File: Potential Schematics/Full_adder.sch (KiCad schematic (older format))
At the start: 5 parts

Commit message: Made Full ALU
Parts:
- gave numbers to parts that had none: 2
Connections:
- net Cin: now also U2.13, U4.10 (IN2); no longer U2.2, U4.2 (IN2)
- net Cout: now also U4.11 (OUT); no longer U4.3 (OUT)
- net S: now also U4.8 (OUT); no longer U4.3 (OUT)
- net a: now also U2.9, U4.4 (IN1); no longer U2.1, U4.1 (IN1)
- net b: now also U2.10, U4.5 (IN2); no longer U2.2, U4.2 (IN2)
- new net: U2.8, U4.13 (IN2)
- new net: U2.12, U4.6 (OUT), U4.9 (IN1)
- new net: U2.11, U4.12 (IN1)
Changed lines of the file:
@@
 $Descr A4 11693 8268
 encoding utf-8
-Sheet 4 6
+Sheet 8 22
 Title "Full-Adder"
 Date ""
@@
 $Comp
 L 74LS08 U?
-U 1 1 5B98F241
+U 3 1 5B98F241
 P 3800 4700
 AR Path="/5B987476/5B988F04/5B98F241" Ref="U?"  Part="1"
-AR Path="/5B990C59/5B990C5E/5B988F04/5B98F241" Ref="U?"  Part="1"
-F 0 "U?" H 3800 4750 50  0000 C CNN
+AR Path="/5B990C59/5B990C5E/5B988F04/5B98F241" Ref="U2"  Part="2"
+AR Path="/5B990C59/5B99BC00/5B988F04/5B98F241" Ref="U5"  Part="3"
+AR Path="/5B990C59/5B99C896/5B988F04/5B98F241" Ref="U13"  Part="4"
+AR Path="/5B990C59/5B99C8B8/5B988F04/5B98F241" Ref="U28"  Part="1"
+F 0 "U5" H 3800 4750 50  0000 C CNN
 F 1 "74LS08" H 3800 4650 50  0000 C CNN
 F 2 "" H 3800 4700 50  0001 C CNN
 F 3 "" H 3800 4700 50  0001 C CNN
-	1    3800 4700
+	3    3800 4700
 	1    0    0    -1
 $EndComp
 $Comp
 L 74LS86 U?
-U 1 1 5B98F2D0
+U 2 1 5B98F2D0
 P 3800 2950
 AR Path="/5B987476/5B988F04/5B98F2D0" Ref="U?"  Part="1"
-AR Path="/5B990C59/5B990C5E/5B988F04/5B98F2D0" Ref="U?"  Part="1"
-F 0 "U?" H 3850 3000 50  0000 C CNN
+AR Path="/5B990C59/5B990C5E/5B988F04/5B98F2D0" Ref="U4"  Part="2"
+AR Path="/5B990C59/5B99BC00/5B988F04/5B98F2D0" Ref="U12"  Part="2"
+AR Path="/5B990C59/5B99C896/5B988F04/5B98F2D0" Ref="U20"  Part="2"
+AR Path="/5B990C59/5B99C8B8/5B988F04/5B98F2D0" Ref="U27"  Part="2"
+F 0 "U12" H 3850 3000 50  0000 C CNN
 F 1 "74LS86" H 3850 2900 50  0000 C CNN
 F 2 "" H 3800 2950 50  0001 C CNN
 F 3 "" H 3800 2950 50  0001 C CNN
-	1    3800 2950
+	2    3800 2950
 	1    0    0    -1
 $EndComp
 $Comp
 L 74LS08 U?
-U 1 1 5B98F473
+U 4 1 5B98F473
 P 6150 3850
 AR Path="/5B987476/5B988F04/5B98F473" Ref="U?"  Part="1"
-AR Path="/5B990C59/5B990C5E/5B988F04/5B98F473" Ref="U?"  Part="1"
-F 0 "U?" H 6150 3900 50  0000 C CNN
+AR Path="/5B990C59/5B990C5E/5B988F04/5B98F473" Ref="U2"  Part="3"
+AR Path="/5B990C59/5B99BC00/5B988F04/5B98F473" Ref="U5"  Part="4"
+AR Path="/5B990C59/5B99C896/5B988F04/5B98F473" Ref="U21"  Part="1"
+AR Path="/5B990C59/5B99C8B8/5B988F04/5B98F473" Ref="U28"  Part="2"
+F 0 "U5" H 6150 3900 50  0000 C CNN
 F 1 "74LS08" H 6150 3800 50  0000 C CNN
 F 2 "" H 6150 3850 50  0001 C CNN
 F 3 "" H 6150 3850 50  0001 C CNN
-	1    6150 3850
+	4    6150 3850
 	1    0    0    -1
 $EndComp
 $Comp
 L 74LS86 U?
-U 1 1 5B98F47A
+U 3 1 5B98F47A
 P 8900 2800
 AR Path="/5B987476/5B988F04/5B98F47A" Ref="U?"  Part="1"
-AR Path="/5B990C59/5B990C5E/5B988F04/5B98F47A" Ref="U?"  Part="1"
-F 0 "U?" H 8950 2850 50  0000 C CNN
+AR Path="/5B990C59/5B990C5E/5B988F04/5B98F47A" Ref="U4"  Part="3"
+AR Path="/5B990C59/5B99BC00/5B988F04/5B98F47A" Ref="U12"  Part="3"
+AR Path="/5B990C59/5B99C896/5B988F04/5B98F47A" Ref="U20"  Part="3"
+AR Path="/5B990C59/5B99C8B8/5B988F04/5B98F47A" Ref="U27"  Part="3"
+F 0 "U12" H 8950 2850 50  0000 C CNN
 F 1 "74LS86" H 8950 2750 50  0000 C CNN
 F 2 "" H 8900 2800 50  0001 C CNN
 F 3 "" H 8900 2800 50  0001 C CNN
-	1    8900 2800
+	3    8900 2800
 	1    0    0    -1
 $EndComp
@@
 $Comp
 L 74LS86 U?
-U 1 1 5B98FB4D
+U 4 1 5B98FB4D
 P 8900 4200
 AR Path="/5B987476/5B988F04/5B98FB4D" Ref="U?"  Part="1"
-AR Path="/5B990C59/5B990C5E/5B988F04/5B98FB4D" Ref="U?"  Part="1"
-F 0 "U?" H 8950 4250 50  0000 C CNN
+AR Path="/5B990C59/5B990C5E/5B988F04/5B98FB4D" Ref="U4"  Part="4"
+AR Path="/5B990C59/5B99BC00/5B988F04/5B98FB4D" Ref="U12"  Part="4"
+AR Path="/5B990C59/5B99C896/5B988F04/5B98FB4D" Ref="U20"  Part="4"
+AR Path="/5B990C59/5B99C8B8/5B988F04/5B98FB4D" Ref="U27"  Part="4"
+F 0 "U12" H 8950 4250 50  0000 C CNN
 F 1 "74LS86" H 8950 4150 50  0000 C CNN
 F 2 "" H 8900 4200 50  0001 C CNN
 F 3 "" H 8900 4200 50  0001 C CNN
-	1    8900 4200
+	4    8900 4200
 	1    0    0    -1
 $EndComp

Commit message: Adding Multiply Devide
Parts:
- U2: symbol 74LS08 -> 4-bit_processor-rescue:74LS08
- U4: symbol 74LS86 -> 4-bit_processor-rescue:74LS86
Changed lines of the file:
@@
-EESchema Schematic File Version 2
-LIBS:power
-LIBS:device
-LIBS:switches
-LIBS:relays
-LIBS:motors
-LIBS:transistors
-LIBS:conn
-LIBS:linear
-LIBS:regul
-LIBS:74xx
-LIBS:cmos4000
-LIBS:adc-dac
-LIBS:memory
-LIBS:xilinx
-LIBS:microcontrollers
-LIBS:dsp
-LIBS:microchip
-LIBS:analog_switches
-LIBS:motorola
-LIBS:texas
-LIBS:intel
-LIBS:audio
-LIBS:interface
-LIBS:digital-audio
-LIBS:philips
-LIBS:display
-LIBS:cypress
-LIBS:siliconi
-LIBS:opto
-LIBS:atmel
-LIBS:contrib
-LIBS:valves
+EESchema Schematic File Version 4
 LIBS:4-bit_processor-cache
-EELAYER 25 0
+EELAYER 26 0
 EELAYER END
 $Descr A4 11693 8268
 encoding utf-8
-Sheet 8 449
+Sheet 8 451
 Title "Full-Adder"
 Date "2018-09-14"
@@
 $EndDescr
 $Comp
-L 74LS08 U?
+L 4-bit_processor-rescue:74LS08 U?
 U 3 1 5B98F241
 P 3800 4700
@@
 $EndComp
 $Comp
-L 74LS86 U?
+L 4-bit_processor-rescue:74LS86 U?
 U 2 1 5B98F2D0
 P 3800 2950
@@
 $EndComp
 $Comp
-L 74LS08 U?
+L 4-bit_processor-rescue:74LS08 U?
 U 4 1 5B98F473
 P 6150 3850
@@
 $EndComp
 $Comp
-L 74LS86 U?
+L 4-bit_processor-rescue:74LS86 U?
 U 3 1 5B98F47A
 P 8900 2800
@@
 Connection ~ 4950 2950
 $Comp
-L 74LS86 U?
+L 4-bit_processor-rescue:74LS86 U?
 U 4 1 5B98FB4D
 P 8900 4200

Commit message: Finished PCB
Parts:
- U1: renamed from U2; footprint (none) -> Daniel_Kopp:DIP-14_300_ELL
- U4: footprint (none) -> Daniel_Kopp:DIP-14_300_ELL
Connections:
- net Cin: now also U1.5; no longer U1.13
- net a: now also U1.1; no longer U1.9
- net b: now also U1.2; no longer U1.10
- net at U4.13 (IN2): now also U1.3; no longer U1.8
- net at U4.6 (OUT), U4.9 (IN1): now also U1.4; no longer U1.12
- net at U4.12 (IN1): now also U1.6; no longer U1.11

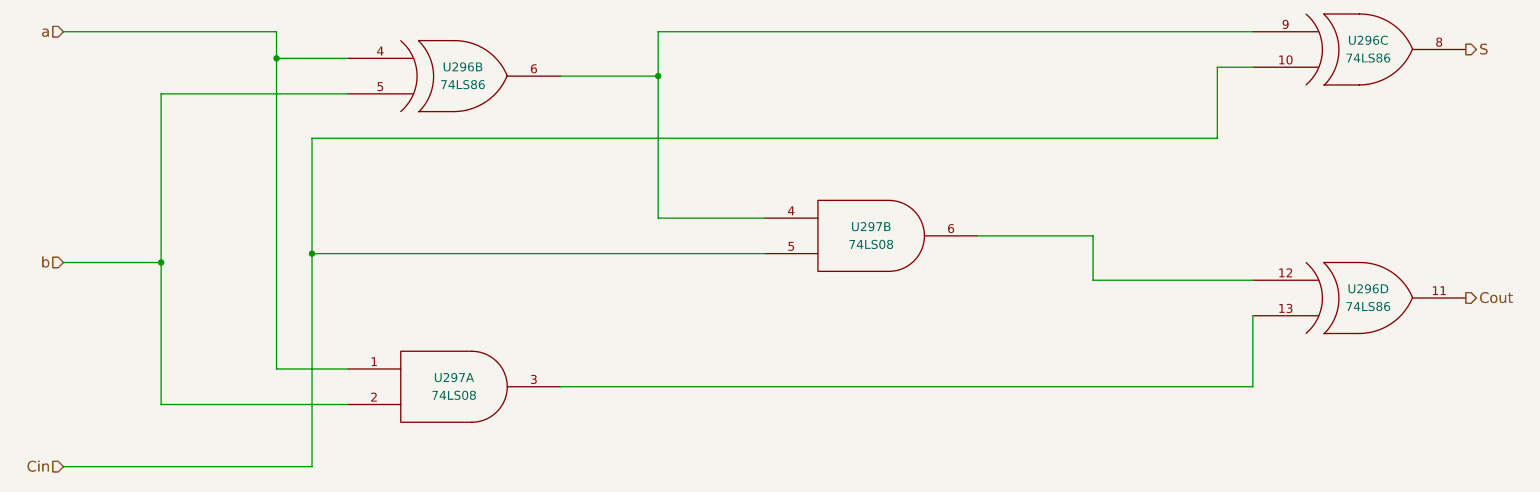
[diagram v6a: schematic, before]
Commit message: Updated overview of Schematic
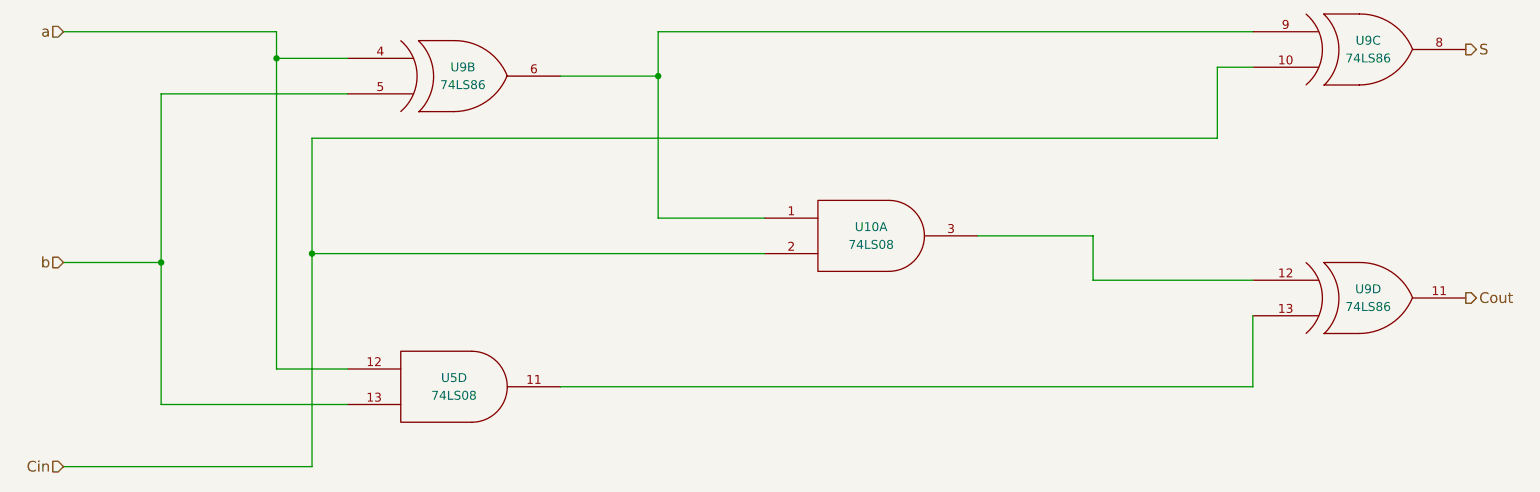
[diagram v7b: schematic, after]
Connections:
- net Cin: now also U1.2; no longer U1.5
- net a: now also U1.12; no longer U1.1
- net b: now also U1.13; no longer U1.2
- net at U4.13 (IN2): now also U1.11; no longer U1.3
- net at U4.6 (OUT), U4.9 (IN1): now also U1.1; no longer U1.4
- net at U4.12 (IN1): now also U1.3; no longer U1.6
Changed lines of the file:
@@
 $Descr A4 11693 8268
 encoding utf-8
-Sheet 452 467
+Sheet 9 902
 Title "Full-Adder"
 Date "2018-09-14"
@@
 $Comp
 L 4-bit_processor-rescue:74LS08 U?
-U 1 1 5B98F241
+U 4 1 5B98F241
 P 3800 4700
 AR Path="/5B987476/5B988F04/5B98F241" Ref="U?"  Part="1"
@@
 AR Path="/5B9D167A/5B9D1E00/5B99C896/5B988F04/5B98F241" Ref="U15"  Part="1"
 AR Path="/5B9D167A/5B9D1E00/5B99C8B8/5B988F04/5B98F241" Ref="U19"  Part="2"
-AR Path="/5B9D167A/5BAA33A0/5BA1B69F/5BA1B9AF/5B98F241" Ref="U291"  Part="3"
-AR Path="/5B9D167A/5BAA33A0/5BA1B69F/5BA1B9B7/5B98F241" Ref="U294"  Part="1"
-AR Path="/5B9D167A/5BAA33A0/5BA1B69F/5BA1B9BF/5B98F241" Ref="U294"  Part="3"
-AR Path="/5B9D167A/5BAA33A0/5BA1B69F/5BA1B9CD/5B98F241" Ref="U297"  Part="1"
-AR Path="/5B9D167A/5BAA33A0/5BAA8A64/5BAA8A92/5B98F241" Ref="U297"  Part="1"
-AR Path="/5B9D167A/5BAA33A0/5BAAD051/5B98F241" Ref="U297"  Part="1"
-F 0 "U297" H 3800 4750 50  0000 C CNN
+AR Path="/5B9D167A/5BAA33A0/5BA1B69F/5BA1B9AF/5B98F241" Ref="U?"  Part="3"
+AR Path="/5B9D167A/5BAA33A0/5BA1B69F/5BA1B9B7/5B98F241" Ref="U?"  Part="1"
+AR Path="/5B9D167A/5BAA33A0/5BA1B69F/5BA1B9BF/5B98F241" Ref="U?"  Part="3"
+AR Path="/5B9D167A/5BAA33A0/5BA1B69F/5BA1B9CD/5B98F241" Ref="U?"  Part="1"
+AR Path="/5B9D167A/5BAA33A0/5BAA8A64/5BAA8A92/5B98F241" Ref="U?"  Part="1"
+AR Path="/5B9D167A/5BAA33A0/5BAAD051/5B98F241" Ref="U?"  Part="1"
+AR Path="/5B9D167A/5BAA33A0/5BAFDB78/5BAFDE3D/5BAAD4A8/5B98F241" Ref="U299"  Part="2"
+AR Path="/5B9D167A/5BAA33A0/5BAFDB78/5BAFDE46/5BABD833/5B98F241" Ref="U299"  Part="4"
+F 0 "U5" H 3800 4750 50  0000 C CNN
 F 1 "74LS08" H 3800 4650 50  0000 C CNN
 F 2 "Daniel_Kopp:DIP-14_300_ELL" H 3800 4700 50  0001 C CNN
 F 3 "" H 3800 4700 50  0001 C CNN
-	1    3800 4700
+	4    3800 4700
 	1    0    0    -1
 $EndComp
@@
 AR Path="/5B9D167A/5B9D1E00/5B99C896/5B988F04/5B98F2D0" Ref="U14"  Part="2"
 AR Path="/5B9D167A/5B9D1E00/5B99C8B8/5B988F04/5B98F2D0" Ref="U20"  Part="2"
-AR Path="/5B9D167A/5BAA33A0/5BA1B69F/5BA1B9AF/5B98F2D0" Ref="U293"  Part="1"
-AR Path="/5B9D167A/5BAA33A0/5BA1B69F/5BA1B9B7/5B98F2D0" Ref="U293"  Part="4"
-AR Path="/5B9D167A/5BAA33A0/5BA1B69F/5BA1B9BF/5B98F2D0" Ref="U295"  Part="3"
-AR Path="/5B9D167A/5BAA33A0/5BA1B69F/5BA1B9CD/5B98F2D0" Ref="U296"  Part="2"
-AR Path="/5B9D167A/5BAA33A0/5BAA8A64/5BAA8A92/5B98F2D0" Ref="U296"  Part="2"
-AR Path="/5B9D167A/5BAA33A0/5BAAD051/5B98F2D0" Ref="U296"  Part="2"
-F 0 "U296" H 3850 3000 50  0000 C CNN
+AR Path="/5B9D167A/5BAA33A0/5BA1B69F/5BA1B9AF/5B98F2D0" Ref="U?"  Part="1"
+AR Path="/5B9D167A/5BAA33A0/5BA1B69F/5BA1B9B7/5B98F2D0" Ref="U?"  Part="4"
+AR Path="/5B9D167A/5BAA33A0/5BA1B69F/5BA1B9BF/5B98F2D0" Ref="U?"  Part="3"
+AR Path="/5B9D167A/5BAA33A0/5BA1B69F/5BA1B9CD/5B98F2D0" Ref="U?"  Part="2"
+AR Path="/5B9D167A/5BAA33A0/5BAA8A64/5BAA8A92/5B98F2D0" Ref="U?"  Part="2"
+AR Path="/5B9D167A/5BAA33A0/5BAAD051/5B98F2D0" Ref="U?"  Part="2"
+AR Path="/5B9D167A/5BAA33A0/5BAFDB78/5BAFDE3D/5BAAD4A8/5B98F2D0" Ref="U300"  Part="1"
+AR Path="/5B9D167A/5BAA33A0/5BAFDB78/5BAFDE46/5BABD833/5B98F2D0" Ref="U300"  Part="4"
+F 0 "U9" H 3850 3000 50  0000 C CNN
 F 1 "74LS86" H 3850 2900 50  0000 C CNN
 F 2 "Daniel_Kopp:DIP-14_300_ELL" H 3800 2950 50  0001 C CNN
@@
 $Comp
 L 4-bit_processor-rescue:74LS08 U?
-U 2 1 5B98F473
+U 1 1 5B98F473
 P 6150 3850
 AR Path="/5B987476/5B988F04/5B98F473" Ref="U?"  Part="1"
@@
 AR Path="/5B9D167A/5B9D1E00/5B99C896/5B988F04/5B98F473" Ref="U15"  Part="2"
 AR Path="/5B9D167A/5B9D1E00/5B99C8B8/5B988F04/5B98F473" Ref="U19"  Part="3"
-AR Path="/5B9D167A/5BAA33A0/5BA1B69F/5BA1B9AF/5B98F473" Ref="U291"  Part="4"
-AR Path="/5B9D167A/5BAA33A0/5BA1B69F/5BA1B9B7/5B98F473" Ref="U294"  Part="2"
-AR Path="/5B9D167A/5BAA33A0/5BA1B69F/5BA1B9BF/5B98F473" Ref="U294"  Part="4"
-AR Path="/5B9D167A/5BAA33A0/5BA1B69F/5BA1B9CD/5B98F473" Ref="U297"  Part="2"
-AR Path="/5B9D167A/5BAA33A0/5BAA8A64/5BAA8A92/5B98F473" Ref="U297"  Part="2"
-AR Path="/5B9D167A/5BAA33A0/5BAAD051/5B98F473" Ref="U297"  Part="2"
-F 0 "U297" H 6150 3900 50  0000 C CNN
+AR Path="/5B9D167A/5BAA33A0/5BA1B69F/5BA1B9AF/5B98F473" Ref="U?"  Part="4"
+AR Path="/5B9D167A/5BAA33A0/5BA1B69F/5BA1B9B7/5B98F473" Ref="U?"  Part="2"
+AR Path="/5B9D167A/5BAA33A0/5BA1B69F/5BA1B9BF/5B98F473" Ref="U?"  Part="4"
+AR Path="/5B9D167A/5BAA33A0/5BA1B69F/5BA1B9CD/5B98F473" Ref="U?"  Part="2"
+AR Path="/5B9D167A/5BAA33A0/5BAA8A64/5BAA8A92/5B98F473" Ref="U?"  Part="2"
+AR Path="/5B9D167A/5BAA33A0/5BAAD051/5B98F473" Ref="U?"  Part="2"
+AR Path="/5B9D167A/5BAA33A0/5BAFDB78/5BAFDE3D/5BAAD4A8/5B98F473" Ref="U299"  Part="3"
+AR Path="/5B9D167A/5BAA33A0/5BAFDB78/5BAFDE46/5BABD833/5B98F473" Ref="U302"  Part="1"
+F 0 "U10" H 6150 3900 50  0000 C CNN
 F 1 "74LS08" H 6150 3800 50  0000 C CNN
 F 2 "Daniel_Kopp:DIP-14_300_ELL" H 6150 3850 50  0001 C CNN
 F 3 "" H 6150 3850 50  0001 C CNN
-	2    6150 3850
+	1    6150 3850
 	1    0    0    -1
 $EndComp
@@
 AR Path="/5B9D167A/5B9D1E00/5B99C896/5B988F04/5B98F47A" Ref="U14"  Part="3"
 AR Path="/5B9D167A/5B9D1E00/5B99C8B8/5B988F04/5B98F47A" Ref="U20"  Part="3"
-AR Path="/5B9D167A/5BAA33A0/5BA1B69F/5BA1B9AF/5B98F47A" Ref="U293"  Part="2"
-AR Path="/5B9D167A/5BAA33A0/5BA1B69F/5BA1B9B7/5B98F47A" Ref="U295"  Part="1"
-AR Path="/5B9D167A/5BAA33A0/5BA1B69F/5BA1B9BF/5B98F47A" Ref="U295"  Part="4"
-AR Path="/5B9D167A/5BAA33A0/5BA1B69F/5BA1B9CD/5B98F47A" Ref="U296"  Part="3"
-AR Path="/5B9D167A/5BAA33A0/5BAA8A64/5BAA8A92/5B98F47A" Ref="U296"  Part="3"
-AR Path="/5B9D167A/5BAA33A0/5BAAD051/5B98F47A" Ref="U296"  Part="3"
-F 0 "U296" H 8950 2850 50  0000 C CNN
+AR Path="/5B9D167A/5BAA33A0/5BA1B69F/5BA1B9AF/5B98F47A" Ref="U?"  Part="2"
+AR Path="/5B9D167A/5BAA33A0/5BA1B69F/5BA1B9B7/5B98F47A" Ref="U?"  Part="1"
+AR Path="/5B9D167A/5BAA33A0/5BA1B69F/5BA1B9BF/5B98F47A" Ref="U?"  Part="4"
+AR Path="/5B9D167A/5BAA33A0/5BA1B69F/5BA1B9CD/5B98F47A" Ref="U?"  Part="3"
+AR Path="/5B9D167A/5BAA33A0/5BAA8A64/5BAA8A92/5B98F47A" Ref="U?"  Part="3"
+AR Path="/5B9D167A/5BAA33A0/5BAAD051/5B98F47A" Ref="U?"  Part="3"
+AR Path="/5B9D167A/5BAA33A0/5BAFDB78/5BAFDE3D/5BAAD4A8/5B98F47A" Ref="U300"  Part="2"
+AR Path="/5B9D167A/5BAA33A0/5BAFDB78/5BAFDE46/5BABD833/5B98F47A" Ref="U303"  Part="1"
+F 0 "U9" H 8950 2850 50  0000 C CNN
 F 1 "74LS86" H 8950 2750 50  0000 C CNN
 F 2 "Daniel_Kopp:DIP-14_300_ELL" H 8900 2800 50  0001 C CNN
@@
 AR Path="/5B9D167A/5B9D1E00/5B99C896/5B988F04/5B98FB4D" Ref="U14"  Part="4"
 AR Path="/5B9D167A/5B9D1E00/5B99C8B8/5B988F04/5B98FB4D" Ref="U20"  Part="4"
-AR Path="/5B9D167A/5BAA33A0/5BA1B69F/5BA1B9AF/5B98FB4D" Ref="U293"  Part="3"
-AR Path="/5B9D167A/5BAA33A0/5BA1B69F/5BA1B9B7/5B98FB4D" Ref="U295"  Part="2"
-AR Path="/5B9D167A/5BAA33A0/5BA1B69F/5BA1B9BF/5B98FB4D" Ref="U296"  Part="1"
-AR Path="/5B9D167A/5BAA33A0/5BA1B69F/5BA1B9CD/5B98FB4D" Ref="U296"  Part="4"
-AR Path="/5B9D167A/5BAA33A0/5BAA8A64/5BAA8A92/5B98FB4D" Ref="U296"  Part="4"
-AR Path="/5B9D167A/5BAA33A0/5BAAD051/5B98FB4D" Ref="U296"  Part="4"
-F 0 "U296" H 8950 4250 50  0000 C CNN
+AR Path="/5B9D167A/5BAA33A0/5BA1B69F/5BA1B9AF/5B98FB4D" Ref="U?"  Part="3"
+AR Path="/5B9D167A/5BAA33A0/5BA1B69F/5BA1B9B7/5B98FB4D" Ref="U?"  Part="2"
+AR Path="/5B9D167A/5BAA33A0/5BA1B69F/5BA1B9BF/5B98FB4D" Ref="U?"  Part="1"
+AR Path="/5B9D167A/5BAA33A0/5BA1B69F/5BA1B9CD/5B98FB4D" Ref="U?"  Part="4"
+AR Path="/5B9D167A/5BAA33A0/5BAA8A64/5BAA8A92/5B98FB4D" Ref="U?"  Part="4"
+AR Path="/5B9D167A/5BAA33A0/5BAAD051/5B98FB4D" Ref="U?"  Part="4"
+AR Path="/5B9D167A/5BAA33A0/5BAFDB78/5BAFDE3D/5BAAD4A8/5B98FB4D" Ref="U300"  Part="3"
+AR Path="/5B9D167A/5BAA33A0/5BAFDB78/5BAFDE46/5BABD833/5B98FB4D" Ref="U303"  Part="2"
+F 0 "U9" H 8950 4250 50  0000 C CNN
 F 1 "74LS86" H 8950 4150 50  0000 C CNN
 F 2 "Daniel_Kopp:DIP-14_300_ELL" H 8900 4200 50  0001 C CNN
